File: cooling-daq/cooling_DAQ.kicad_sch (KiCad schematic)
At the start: 47 parts, among them J1 Conn_02x10_Odd_Even, J1 USB_C_Receptacle_USB2.0_16P, Q1 2N7002, Q2 2N7002, SW1 SW_SPST, U1 STM32F103C8Tx, U2 AP2204K-ADJ, U3 AP2204K-ADJ, U6 SN65HVD256D, Y1 8M, Y2 32.768k

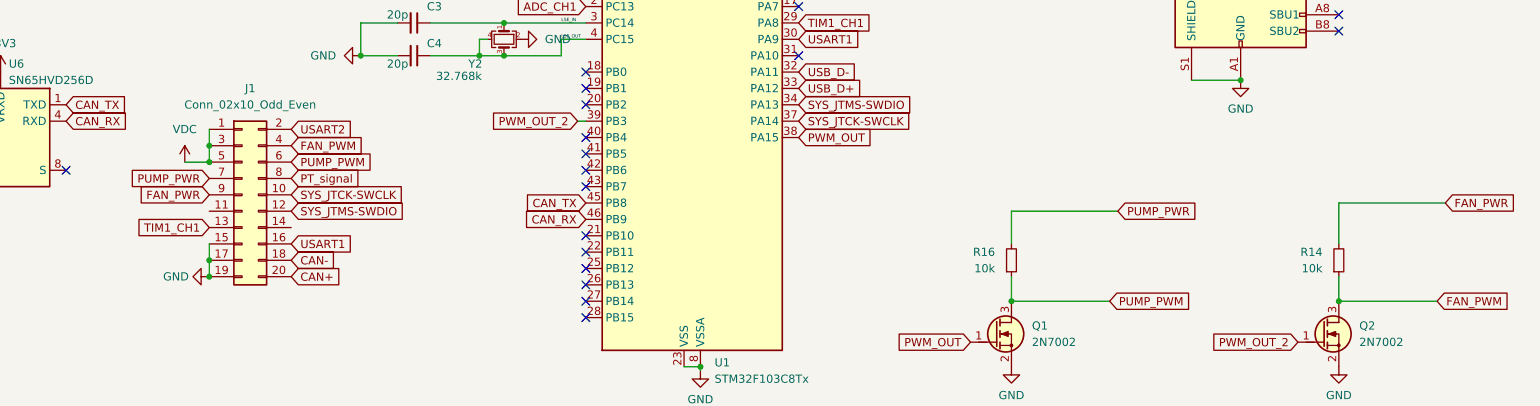
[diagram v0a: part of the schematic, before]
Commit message: fix CAN IC, modify pump_PWR, fix Cu length label
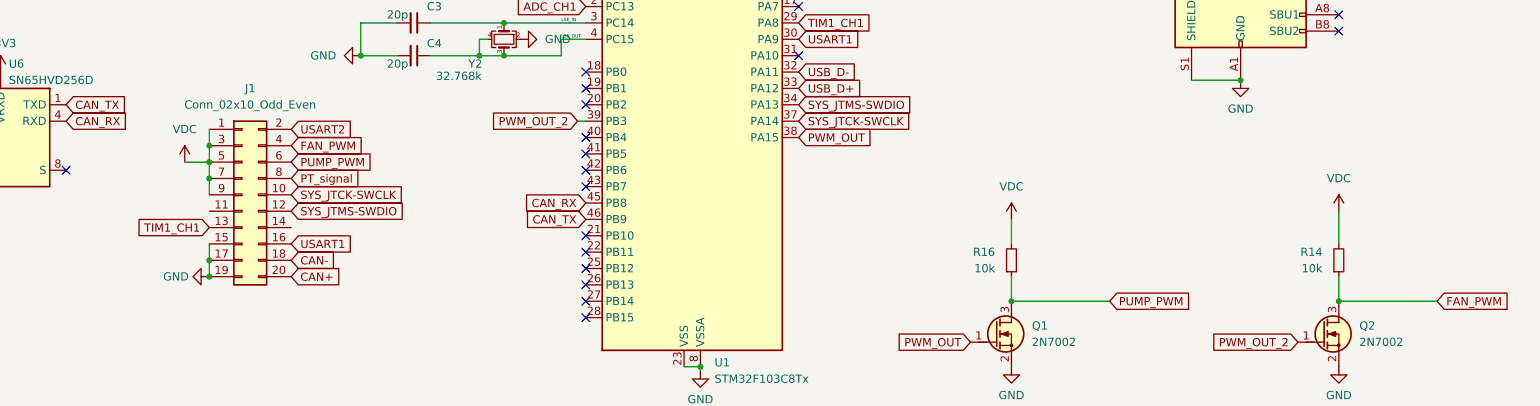
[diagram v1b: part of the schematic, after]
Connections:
- net FAN_PWR is gone; now on net VDC: J1.9 (Pin_9), R14.2
- net PUMP_PWR is gone; now on net VDC: J1.7 (Pin_7), R16.2
- net CAN_RX: now also U1.45 (PB8); no longer U1.46 (PB9)
- net CAN_TX: now also U1.46 (PB9); no longer U1.45 (PB8)
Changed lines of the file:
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@@
   (title_block
     (title "Cooling DAQ")
-    (date "2025-02-05")
+    (date "2025-04-20")
   )
   (junction (at 74.93 121.92) (diameter 0) (color 0 0 0 0)
@@
   )
   (junction (at 151.13 77.47) (diameter 0) (color 0 0 0 0)
+  )
+  (junction (at 74.93 127) (diameter 0) (color 0 0 0 0)
   )
   (junction (at 74.93 124.46) (diameter 0) (color 0 0 0 0)
@@
     (stroke (width 0) (type default))
   )
+  (wire (pts (xy 74.93 124.46) (xy 74.93 127))
+    (stroke (width 0) (type default))
+  )
   (wire (pts (xy 198.12 28.575) (xy 198.12 31.115))
     (stroke (width 0) (type default))
@@
     (stroke (width 0) (type default))
   )
-  (wire (pts (xy 199.39 132.08) (xy 215.9 132.08))
-    (stroke (width 0) (type default))
-  )
   (wire (pts (xy 238.125 33.655) (xy 252.095 33.655))
     (stroke (width 0) (type default))
@@
     (stroke (width 0) (type default))
   )
-  (wire (pts (xy 250.19 130.81) (xy 266.7 130.81))
-    (stroke (width 0) (type default))
-  )
   (wire (pts (xy 215.265 31.115) (xy 222.885 31.115))
     (stroke (width 0) (type default))
@@
     (stroke (width 0) (type default))
   )
+  (wire (pts (xy 74.93 127) (xy 74.93 129.54))
+    (stroke (width 0) (type default))
+  )
   (wire (pts (xy 115.57 96.52) (xy 115.57 92.71))
     (stroke (width 0) (type default))
@@
     (stroke (width 0) (type default))
   )
-  (wire (pts (xy 199.39 137.16) (xy 199.39 132.08))
+  (wire (pts (xy 199.39 137.16) (xy 199.39 133.35))
     (stroke (width 0) (type default))
   )
@@
     (stroke (width 0) (type default))
   )
-  (wire (pts (xy 250.19 137.16) (xy 250.19 130.81))
+  (wire (pts (xy 250.19 137.16) (xy 250.19 132.08))
     (stroke (width 0) (type default))
   )
@@
     (property "Intersheetrefs" "${INTERSHEET_REFS}" (at 95.8767 139.7 0)
       (effects (font (size 1.27 1.27)) (justify left) hide)
-    )
-  )
-  (global_label "CAN_RX" (shape input) (at 133.35 133.35 180) (fields_autoplaced)
-    (effects (font (size 1.27 1.27)) (justify right))
-    (property "Intersheetrefs" "${INTERSHEET_REFS}" (at 123.2286 133.35 0)
-      (effects (font (size 1.27 1.27)) (justify right) hide)
     )
   )
@@
     )
   )
-  (global_label "FAN_PWR" (shape input) (at 74.93 129.54 180) (fields_autoplaced)
-    (effects (font (size 1.27 1.27)) (justify right))
-    (property "Intersheetrefs" "${INTERSHEET_REFS}" (at 63.4781 129.54 0)
-      (effects (font (size 1.27 1.27)) (justify right) hide)
-    )
-  )
   (global_label "ADC_CH1" (shape input) (at 133.35 100.33 180) (fields_autoplaced)
     (effects (font (size 1.27 1.27)) (justify right))
@@
     )
   )
-  (global_label "CAN_TX" (shape input) (at 133.35 130.81 180) (fields_autoplaced)
-    (effects (font (size 1.27 1.27)) (justify right))
-    (property "Intersheetrefs" "${INTERSHEET_REFS}" (at 123.531 130.81 0)
-      (effects (font (size 1.27 1.27)) (justify right) hide)
-    )
-  )
   (global_label "USART1" (shape input) (at 60.96 29.21 90) (fields_autoplaced)
     (effects (font (size 1.27 1.27)) (justify left))
@@
     )
   )
-  (global_label "PUMP_PWR" (shape input) (at 74.93 127 180) (fields_autoplaced)
+  (global_label "CAN_RX" (shape input) (at 133.35 130.81 180) (fields_autoplaced)
     (effects (font (size 1.27 1.27)) (justify right))
-    (property "Intersheetrefs" "${INTERSHEET_REFS}" (at 61.6639 127 0)
+    (property "Intersheetrefs" "${INTERSHEET_REFS}" (at 123.2286 130.81 0)
       (effects (font (size 1.27 1.27)) (justify right) hide)
-    )
-  )
-  (global_label "FAN_PWR" (shape input) (at 266.7 130.81 0) (fields_autoplaced)
-    (effects (font (size 1.27 1.27)) (justify left))
-    (property "Intersheetrefs" "${INTERSHEET_REFS}" (at 278.1519 130.81 0)
-      (effects (font (size 1.27 1.27)) (justify left) hide)
     )
   )
@@
     )
   )
+  (global_label "CAN_TX" (shape input) (at 133.35 133.35 180) (fields_autoplaced)
+    (effects (font (size 1.27 1.27)) (justify right))
+    (property "Intersheetrefs" "${INTERSHEET_REFS}" (at 123.531 133.35 0)
+      (effects (font (size 1.27 1.27)) (justify right) hide)
+    )
+  )
   (global_label "SYS_JTCK-SWCLK" (shape input) (at 87.63 129.54 0) (fields_autoplaced)
     (effects (font (size 1.27 1.27)) (justify left))
@@
     (effects (font (size 1.27 1.27)) (justify left))
     (property "Intersheetrefs" "${INTERSHEET_REFS}" (at 176.9752 113.03 0)
-      (effects (font (size 1.27 1.27)) (justify left) hide)
-    )
-  )
-  (global_label "PUMP_PWR" (shape input) (at 215.9 132.08 0) (fields_autoplaced)
-    (effects (font (size 1.27 1.27)) (justify left))
-    (property "Intersheetrefs" "${INTERSHEET_REFS}" (at 229.1661 132.08 0)
       (effects (font (size 1.27 1.27)) (justify left) hide)
     )
@@
     )
   )
+  (symbol (lib_id "power:VDC") (at 199.39 133.35 0) (unit 1)
+    (in_bom yes) (on_board yes) (dnp no) (fields_autoplaced)
+    (property "Reference" "#PWR08" (at 199.39 135.89 0)
+      (effects (font (size 1.27 1.27)) hide)
+    )
+    (property "Value" "VDC" (at 199.39 128.27 0)
+      (effects (font (size 1.27 1.27)))
+    )
+    (property "Footprint" "" (at 199.39 133.35 0)
+      (effects (font (size 1.27 1.27)) hide)
+    )
+    (property "Datasheet" "" (at 199.39 133.35 0)
+      (effects (font (size 1.27 1.27)) hide)
+    )
+    (pin "1")
+    (instances
+      (project "cooling_DAQ"
+        (path "/dee19d1a-70c7-4b45-ad92-fd6630db17d6"
+          (reference "#PWR08") (unit 1)
+        )
+      )
+    )
+  )
   (symbol (lib_id "Device:R") (at 60.96 34.29 0) (unit 1)
     (in_bom yes) (on_board yes) (dnp no) (fields_autoplaced)
@@
         )
       )
+    )
+  )
+  (symbol (lib_id "power:VDC") (at 250.19 132.08 0) (unit 1)
+    (in_bom yes) (on_board yes) (dnp no) (fields_autoplaced)
+    (property "Reference" "#PWR09" (at 250.19 134.62 0)
+      (effects (font (size 1.27 1.27)) hide)
+    )
+    (property "Value" "VDC" (at 250.19 127 0)
+      (effects (font (size 1.27 1.27)))
+    )
+    (property "Footprint" "" (at 250.19 132.08 0)
+      (effects (font (size 1.27 1.27)) hide)
+    )
+    (property "Datasheet" "" (at 250.19 132.08 0)
+      (effects (font (size 1.27 1.27)) hide)
+    )
+    (pin "1")
+    (instances
+      (project "cooling_DAQ"
+        (path "/dee19d1a-70c7-4b45-ad92-fd6630db17d6"
+          (reference "#PWR09") (unit 1)
+        )
+      )

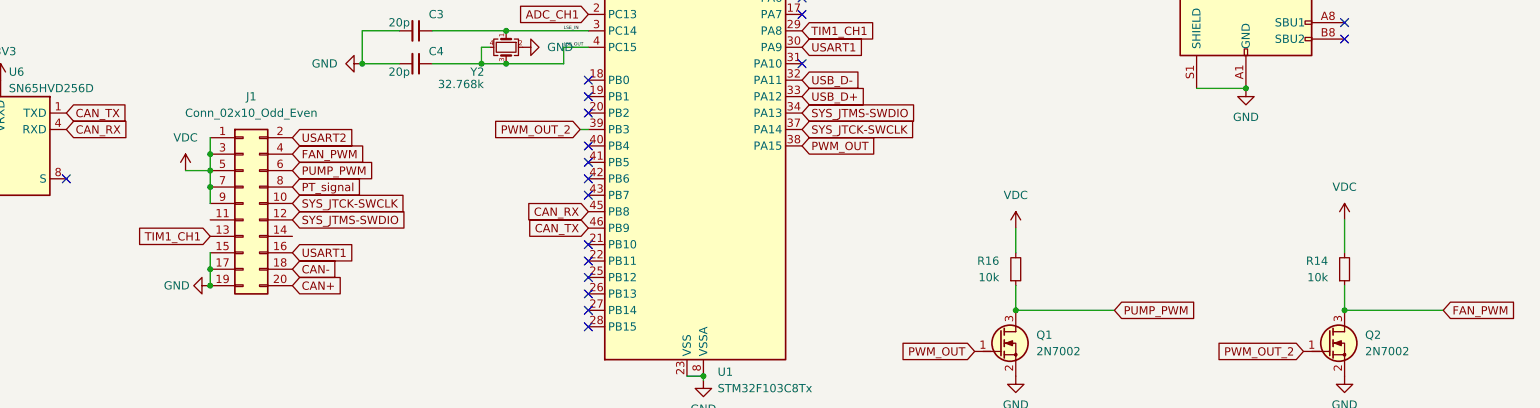
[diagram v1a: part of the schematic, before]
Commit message: recover PUMP_PWR
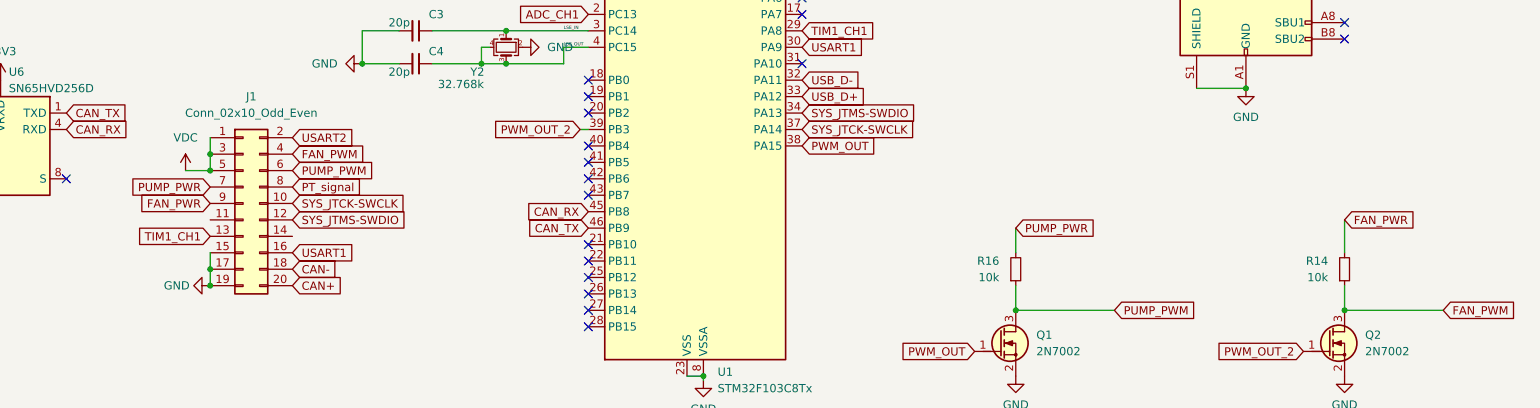
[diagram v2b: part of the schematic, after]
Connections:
- net VDC: no longer J1.7 (Pin_7), J1.9 (Pin_9), R14.2, R16.2
- new net FAN_PWR: J1.9 (Pin_9), R14.2
- new net PUMP_PWR: J1.7 (Pin_7), R16.2
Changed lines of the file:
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@@
   (junction (at 151.13 77.47) (diameter 0) (color 0 0 0 0)
-  )
-  (junction (at 74.93 127) (diameter 0) (color 0 0 0 0)
   )
   (junction (at 74.93 124.46) (diameter 0) (color 0 0 0 0)
@@
     (stroke (width 0) (type default))
   )
-  (wire (pts (xy 74.93 124.46) (xy 74.93 127))
-    (stroke (width 0) (type default))
-  )
   (wire (pts (xy 198.12 28.575) (xy 198.12 31.115))
     (stroke (width 0) (type default))
@@
   )
   (wire (pts (xy 74.93 139.7) (xy 74.93 142.24))
-    (stroke (width 0) (type default))
-  )
-  (wire (pts (xy 74.93 127) (xy 74.93 129.54))
     (stroke (width 0) (type default))
   )
@@
     (property "Intersheetrefs" "${INTERSHEET_REFS}" (at 95.8767 139.7 0)
       (effects (font (size 1.27 1.27)) (justify left) hide)
+    )
+  )
+  (global_label "FAN_PWR" (shape input) (at 74.93 129.54 180) (fields_autoplaced)
+    (effects (font (size 1.27 1.27)) (justify right))
+    (property "Intersheetrefs" "${INTERSHEET_REFS}" (at 63.4781 129.54 0)
+      (effects (font (size 1.27 1.27)) (justify right) hide)
     )
   )
@@
     )
   )
+  (global_label "PUMP_PWR" (shape input) (at 199.39 133.35 0) (fields_autoplaced)
+    (effects (font (size 1.27 1.27)) (justify left))
+    (property "Intersheetrefs" "${INTERSHEET_REFS}" (at 212.6561 133.35 0)
+      (effects (font (size 1.27 1.27)) (justify left) hide)
+    )
+  )
   (global_label "USB_D-" (shape input) (at 166.37 110.49 0) (fields_autoplaced)
     (effects (font (size 1.27 1.27)) (justify left))
@@
     (property "Intersheetrefs" "${INTERSHEET_REFS}" (at 186.107 118.11 0)
       (effects (font (size 1.27 1.27)) (justify left) hide)
+    )
+  )
+  (global_label "PUMP_PWR" (shape input) (at 74.93 127 180) (fields_autoplaced)
+    (effects (font (size 1.27 1.27)) (justify right))
+    (property "Intersheetrefs" "${INTERSHEET_REFS}" (at 61.6639 127 0)
+      (effects (font (size 1.27 1.27)) (justify right) hide)
     )
   )
@@
     (property "Intersheetrefs" "${INTERSHEET_REFS}" (at 19.0583 123.19 0)
       (effects (font (size 1.27 1.27)) (justify right) hide)
+    )
+  )
+  (global_label "FAN_PWR" (shape input) (at 250.19 132.08 0) (fields_autoplaced)
+    (effects (font (size 1.27 1.27)) (justify left))
+    (property "Intersheetrefs" "${INTERSHEET_REFS}" (at 261.6419 132.08 0)
+      (effects (font (size 1.27 1.27)) (justify left) hide)
     )
   )
@@
     )
   )
-  (symbol (lib_id "power:VDC") (at 199.39 133.35 0) (unit 1)
-    (in_bom yes) (on_board yes) (dnp no) (fields_autoplaced)
-    (property "Reference" "#PWR08" (at 199.39 135.89 0)
-      (effects (font (size 1.27 1.27)) hide)
-    )
-    (property "Value" "VDC" (at 199.39 128.27 0)
-      (effects (font (size 1.27 1.27)))
-    )
-    (property "Footprint" "" (at 199.39 133.35 0)
-      (effects (font (size 1.27 1.27)) hide)
-    )
-    (property "Datasheet" "" (at 199.39 133.35 0)
-      (effects (font (size 1.27 1.27)) hide)
-    )
-    (pin "1")
-    (instances
-      (project "cooling_DAQ"
-        (path "/dee19d1a-70c7-4b45-ad92-fd6630db17d6"
-          (reference "#PWR08") (unit 1)
-        )
-      )
-    )
-  )
   (symbol (lib_id "Device:R") (at 60.96 34.29 0) (unit 1)
     (in_bom yes) (on_board yes) (dnp no) (fields_autoplaced)
@@
         )
       )
-    )
-  )
-  (symbol (lib_id "power:VDC") (at 250.19 132.08 0) (unit 1)
-    (in_bom yes) (on_board yes) (dnp no) (fields_autoplaced)
-    (property "Reference" "#PWR09" (at 250.19 134.62 0)
-      (effects (font (size 1.27 1.27)) hide)
-    )
-    (property "Value" "VDC" (at 250.19 127 0)
-      (effects (font (size 1.27 1.27)))
-    )
-    (property "Footprint" "" (at 250.19 132.08 0)
-      (effects (font (size 1.27 1.27)) hide)
-    )
-    (property "Datasheet" "" (at 250.19 132.08 0)
-      (effects (font (size 1.27 1.27)) hide)
-    )
-    (pin "1")
-    (instances
-      (project "cooling_DAQ"
-        (path "/dee19d1a-70c7-4b45-ad92-fd6630db17d6"
-          (reference "#PWR09") (unit 1)
-        )
-      )

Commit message: v2025.10 :user friendly ver.
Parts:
- added D1: ~, LED_SMD:LED_0805_2012Metric, symbol Device:LED_Small
- added D2: BAT46W-7-F, Diode_SMD:D_SOD-123, symbol Diode:1N4148W
- added D3: PWR, LED_SMD:LED_0805_2012Metric, symbol Device:LED_Small
- added J2: Conn_01x03_Pin, Connector_PinHeader_2.54mm:PinHeader_1x03_P2.54mm_Vertical, symbol Connector:Conn_01x03_Pin
- added J3, J4: Conn_01x02_Pin, Connector_PinHeader_2.54mm:PinHeader_1x02_P2.54mm_Vertical, symbol Connector:Conn_01x02_Pin
- added Q3: Si2301CDS, Package_TO_SOT_SMD:SOT-23, symbol Transistor_FET:Si2319CDS
- added R15: 4.7k, Resistor_SMD:R_0603_1608Metric, symbol Device:R
- added R17: 1k, Resistor_SMD:R_0603_1608Metric, symbol Device:R_Small
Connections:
- net +3V3: now also Q3.3 (D)
- net +5V: now also D2.1 (K), J4.1 (Pin_1), R17.1; no longer J1.A4 (VBUS), J1.A9 (VBUS), J1.B4 (VBUS), J1.B9 (VBUS)
- net CAN+: now also J3.1 (Pin_1)
- net CAN-: now also J3.2 (Pin_2)
- net GND: now also D1.1 (K), D3.1 (K), J2.3 (Pin_3), J4.2 (Pin_2)
- net SYS_JTCK-SWCLK: now also J2.2 (Pin_2); no longer J1.10 (Pin_10)
- net SYS_JTMS-SWDIO: now also J2.1 (Pin_1); no longer J1.12 (Pin_12)
- net NRST: now reaches R1.2, SW1.2 (B), U1.7 (NRST)
- net NRST: now also R15.1
- new net: Q3.1 (G), R15.2
- new net: D2.2 (A), J1.A4 (VBUS), J1.A9 (VBUS), J1.B4 (VBUS), J1.B9 (VBUS)
- new net: D1.2 (A), Q3.2 (S)
- new net: D3.2 (A), R17.2
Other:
- moved on the sheet: SW1
